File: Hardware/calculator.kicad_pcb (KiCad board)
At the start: 4 copper layers, 70.5 x 143 mm, 46 parts

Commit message: feat: update calculator engine capabilities, automate PCB manufacturing output, and refine hardware build process
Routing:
- added copper zone on B.Cu, net (none)
- added copper zone on F.Cu, net (none)
- added copper zone on In1.Cu, net (none)
- added copper zone on In2.Cu, net (none)
- removed copper zone on B.Cu, net GND
- removed copper zone on F.Cu, net GND
- removed copper zone on In1.Cu, net GND
- removed copper zone on In2.Cu, net GND

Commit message: feat: implement alpha key input support and unify error handling in RetroUIController
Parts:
- moved Disp 6.00 mm to (29.5, -125.9)
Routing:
- net P21: track 185.1 -> 51.6 mm, vias 3 -> 0
- net P20: track 89.1 -> 131.7 mm, vias 0 -> 3
- net P6: track 162.6 -> 197.1 mm, vias 4 -> 5
- net P1: track 134.6 -> 165.9 mm, vias 5 -> 4
- net P4: track 109.3 -> 132.8 mm, vias 6 -> 4
- net P10: track 173.3 -> 195.4 mm, vias 3 -> 4
- net P5: track 145.5 -> 167.1 mm, vias 3 -> 4
- net P14: track 135.2 -> 153.6 mm, vias 2 -> 1
- net P18: track 1.74 -> 19.9 mm
- net P16: track 86.2 -> 103.8 mm, vias 2 -> 1
- net GND: track 54.9 -> 67.0 mm, vias 1 -> 0
- net P0: track 129.8 -> 141.5 mm
- net P15: track 133.2 -> 142.1 mm, vias 2 -> 1
- net P9: track 141.7 -> 148.4 mm, vias 2 -> 1
- net P7: track 148.7 -> 155.3 mm, vias 2 -> 1
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- added copper zone on B.Cu, net GND
- added copper zone on F.Cu, net GND
- removed copper zone on B.Cu, net (none)
- removed copper zone on F.Cu, net (none)
- removed copper zone on In1.Cu, net (none)
- removed copper zone on In2.Cu, net (none)
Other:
- copper layers 4 -> 2

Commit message: refactor: update UI layout, adjust font rendering, and modify PCB hardware footprint configuration
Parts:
- B1, B10, B11, B12, B13, B14, B15, B16, B17, B18, B19, B2, B20, B21, B22, B23, B24, B25, B26, B27, B28, B29, B3, B30, B31, B32, B33, B34, B35, B36, B37, B4, B5, B6, B7, B8, B9: value (none) -> Tactile Switch 6x6mm
- JST1: value (none) -> JST-PH 2.0 2-Pin
- MCU1: value (none) -> RASPBERRY PI PICO
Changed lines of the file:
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@@
 	(footprint "E73:SW_TACT_ALPS_SKQGABE010"
 		(layer "F.Cu")
-		(at 17.525 -32.924999)
+		(at 39.525 -32.924999)
 		(descr "Low-profile SMD Tactile Switch, https://www.e-switch.com/product-catalog/tact/product-lines/tl3342-series-low-profile-smt-tact-switch")
 		(tags "SPST Tactile Switch")
-		(property "Reference" "B20"
+		(property "Reference" "B24"
 			(at 0 0 0)
 			(layer "F.SilkS")
@@
 			)
 		)
-		(property "Value" ""
+		(property "Value" "Tactile Switch 6x6mm"
 			(at 0 0 0)
 			(layer "F.SilkS")
@@
 			(size 1.8 1.1)
 			(layers "F.Cu" "F.Mask" "F.Paste")
-			(net "P7")
+			(net "P8")
 		)
 		(pad "NC" smd rect
@@
 	(footprint "E73:SW_TACT_ALPS_SKQGABE010"
 		(layer "F.Cu")
-		(at 39.525 -32.924999)
+		(at 17.525 -32.924999)
 		(descr "Low-profile SMD Tactile Switch, https://www.e-switch.com/product-catalog/tact/product-lines/tl3342-series-low-profile-smt-tact-switch")
 		(tags "SPST Tactile Switch")
-		(property "Reference" "B24"
+		(property "Reference" "B20"
 			(at 0 0 0)
 			(layer "F.SilkS")
@@
 			)
 		)
-		(property "Value" ""
+		(property "Value" "Tactile Switch 6x6mm"
 			(at 0 0 0)
 			(layer "F.SilkS")
@@
 			(size 1.8 1.1)
 			(layers "F.Cu" "F.Mask" "F.Paste")
-			(net "P8")
+			(net "P7")
 		)
 		(pad "NC" smd rect
@@
 			)
 		)
-		(property "Value" ""
+		(property "Value" "Tactile Switch 6x6mm"
 			(at 0 0 0)
 			(layer "F.SilkS")
@@
 			)
 		)
-		(property "Value" ""
+		(property "Value" "Tactile Switch 6x6mm"
 			(at 0 0 0)
 			(layer "F.SilkS")
@@
 			)
 		)
-		(property "Value" ""
+		(property "Value" "Tactile Switch 6x6mm"
 			(at 0 0 0)
 			(layer "F.SilkS")
@@
 			)
 		)
-		(property "Value" ""
+		(property "Value" "Tactile Switch 6x6mm"
 			(at 0 0 0)
 			(layer "F.SilkS")
@@
 			)
 		)
-		(property "Value" ""
+		(property "Value" "Tactile Switch 6x6mm"
 			(at 0 0 0)
 			(layer "F.SilkS")
@@
 			)
 		)
-		(property "Value" ""
+		(property "Value" "Tactile Switch 6x6mm"
 			(at 0 0 0)
 			(layer "F.SilkS")
@@
 			)
 		)
-		(property "Value" ""
+		(property "Value" "Tactile Switch 6x6mm"
 			(at 0 0 0)
 			(layer "F.SilkS")
@@
 			)
 		)
-		(property "Value" ""
+		(property "Value" "Tactile Switch 6x6mm"
 			(at 0 0 0)
 			(layer "F.SilkS")
@@
 			)
 		)
-		(property "Value" ""
+		(property "Value" "Tactile Switch 6x6mm"
 			(at 0 0 0)
 			(layer "F.SilkS")
@@
 			)
 		)
-		(property "Value" ""
+		(property "Value" "Tactile Switch 6x6mm"
 			(at 0 0 0)
 			(layer "F.SilkS")
@@
 	(footprint "E73:SW_TACT_ALPS_SKQGABE010"
 		(layer "F.Cu")
-		(at 17.525 -56.925)
+		(at 17.525 -44.925)
 		(descr "Low-profile SMD Tactile Switch, https://www.e-switch.com/product-catalog/tact/product-lines/tl3342-series-low-profile-smt-tact-switch")
 		(tags "SPST Tactile Switch")
-		(property "Reference" "B18"
+		(property "Reference" "B19"
 			(at 0 0 0)
 			(layer "F.SilkS")
@@
 			)
 		)
-		(property "Value" ""
+		(property "Value" "Tactile Switch 6x6mm"
 			(at 0 0 0)
 			(layer "F.SilkS")
@@
 			(size 1.8 1.1)
 			(layers "F.Cu" "F.Mask" "F.Paste")
-			(net "P5")
+			(net "P6")
 		)
 		(pad "2" smd rect
@@
 	(footprint "E73:SW_TACT_ALPS_SKQGABE010"
 		(layer "F.Cu")
-		(at 17.525 -44.925)
+		(at 17.525 -20.925)
 		(descr "Low-profile SMD Tactile Switch, https://www.e-switch.com/product-catalog/tact/product-lines/tl3342-series-low-profile-smt-tact-switch")
 		(tags "SPST Tactile Switch")
-		(property "Reference" "B19"
+		(property "Reference" "B21"
 			(at 0 0 0)
 			(layer "F.SilkS")
@@
 			)
 		)
-		(property "Value" ""
+		(property "Value" "Tactile Switch 6x6mm"
 			(at 0 0 0)
 			(layer "F.SilkS")
@@
 			(size 1.8 1.1)
 			(layers "F.Cu" "F.Mask" "F.Paste")
-			(net "P6")
+			(net "P21")
 		)
 		(pad "2" smd rect
@@
 	(footprint "E73:SW_TACT_ALPS_SKQGABE010"
 		(layer "F.Cu")
-		(at 17.525 -20.925)
+		(at 39.525 -56.925)
 		(descr "Low-profile SMD Tactile Switch, https://www.e-switch.com/product-catalog/tact/product-lines/tl3342-series-low-profile-smt-tact-switch")
 		(tags "SPST Tactile Switch")
-		(property "Reference" "B21"
+		(property "Reference" "B22"
 			(at 0 0 0)
 			(layer "F.SilkS")
@@
 			)
 		)
-		(property "Value" ""
+		(property "Value" "Tactile Switch 6x6mm"
 			(at 0 0 0)
 			(layer "F.SilkS")
@@
 			(size 1.8 1.1)
 			(layers "F.Cu" "F.Mask" "F.Paste")
-			(net "P21")
+			(net "P5")
 		)
 		(pad "2" smd rect
@@
 			(size 1.8 1.1)
 			(layers "F.Cu" "F.Mask" "F.Paste")
-			(net "P7")
+			(net "P8")
 		)
 		(pad "NC" smd rect
@@
 	(footprint "E73:SW_TACT_ALPS_SKQGABE010"
 		(layer "F.Cu")
-		(at 39.525 -56.925)
+		(at 17.525 -56.925)
 		(descr "Low-profile SMD Tactile Switch, https://www.e-switch.com/product-catalog/tact/product-lines/tl3342-series-low-profile-smt-tact-switch")
 		(tags "SPST Tactile Switch")
-		(property "Reference" "B22"
+		(property "Reference" "B18"
 			(at 0 0 0)
 			(layer "F.SilkS")
@@
 			)
 		)
-		(property "Value" ""
+		(property "Value" "Tactile Switch 6x6mm"
 			(at 0 0 0)
 			(layer "F.SilkS")
@@
 			(size 1.8 1.1)
 			(layers "F.Cu" "F.Mask" "F.Paste")
-			(net "P8")
+			(net "P7")
 		)
 		(pad "NC" smd rect
@@
 			)
 		)
-		(property "Value" ""
+		(property "Value" "Tactile Switch 6x6mm"
 			(at 0 0 0)
 			(layer "F.SilkS")
@@
 			)
 		)
-		(property "Value" ""
+		(property "Value" "Tactile Switch 6x6mm"
 			(at 0 0 0)
 			(layer "F.SilkS")
@@
 			)
 		)
-		(property "Value" ""
+		(property "Value" "Tactile Switch 6x6mm"
 			(at 0 0 0)
 			(layer "F.SilkS")
@@
 			)
 		)
-		(property "Value" ""
+		(property "Value" "Tactile Switch 6x6mm"
 			(at 0 0 0)
 			(layer "F.SilkS")
@@
 			)
 		)
-		(property "Value" ""
+		(property "Value" "Tactile Switch 6x6mm"
 			(at 0 0 0)
 			(layer "F.SilkS")
@@
 			)
 		)
-		(property "Value" ""
+		(property "Value" "Tactile Switch 6x6mm"
 			(at 0 0 0)
 			(layer "F.SilkS")
@@
 			)
 		)
-		(property "Value" ""
+		(property "Value" "Tactile Switch 6x6mm"
 			(at 0 0 0)
 			(layer "F.SilkS")
@@
 			)
 		)
-		(property "Value" ""
+		(property "Value" "Tactile Switch 6x6mm"
 			(at 0 0 0)
 			(layer "F.SilkS")
@@
 			)
 		)
-		(property "Value" ""
+		(property "Value" "Tactile Switch 6x6mm"
 			(at 0 0 0)
 			(layer "F.SilkS")
@@
 			)
 		)
-		(property "Value" ""
+		(property "Value" "Tactile Switch 6x6mm"
 			(at 0 0 0)
 			(layer "F.SilkS")
@@
 			)
 		)
-		(property "Value" ""
+		(property "Value" "Tactile Switch 6x6mm"
 			(at 0 0 0)
 			(layer "F.SilkS")
@@
 			)
 		)
-		(property "Value" ""
+		(property "Value" "Tactile Switch 6x6mm"
 			(at 0 0 0)
 			(layer "F.SilkS")
@@
 			)
 		)
-		(property "Value" ""
+		(property "Value" "Tactile Switch 6x6mm"
 			(at 0 0 0)
 			(layer "F.SilkS")
@@
 			)
 		)
-		(property "Value" ""
+		(property "Value" "Tactile Switch 6x6mm"
 			(at 0 0 0)
 			(layer "F.SilkS")
@@
 			)
 		)
-		(property "Value" ""
+		(property "Value" "Tactile Switch 6x6mm"
 			(at 0 0 0)
 			(layer "F.SilkS")
@@
 			)
 		)
-		(property "Value" ""
+		(property "Value" "Tactile Switch 6x6mm"
 			(at 0 0 0)
 			(layer "F.SilkS")
@@
 			)
 		)
-		(property "Value" ""
+		(property "Value" "Tactile Switch 6x6mm"
 			(at 0 0 0)
 			(layer "F.SilkS")
@@
 			)
 		)
-		(property "Value" ""
+		(property "Value" "Tactile Switch 6x6mm"
 			(at 0 0 0)
 			(layer "F.SilkS")
@@
 			)
 		)
-		(property "Value" ""
+		(property "Value" "Tactile Switch 6x6mm"
 			(at 0 0 0)
 			(layer "F.SilkS")
@@
 			)
 		)
-		(property "Value" ""
+		(property "Value" "Tactile Switch 6x6mm"
 			(at 0 0 0)
 			(layer "F.SilkS")
@@
 			)
 		)
-		(property "Value" ""
+		(property "Value" "Tactile Switch 6x6mm"
 			(at 0 0 0)
 			(layer "F.SilkS")
@@
 			)
 		)
-		(property "Value" ""
+		(property "Value" "JST-PH 2.0 2-Pin"
 			(at 0 0 0)
 			(layer "B.SilkS")
@@
 			)
 		)
-		(property "Value" ""
+		(property "Value" "RASPBERRY PI PICO"
 			(at 0 0 0)
 			(layer "B.SilkS")

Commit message: refactor: migrate UI display to use dedicated font scaling and add PCBWay manufacturing guidelines and BOM generation improvements
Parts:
- added FID1: Fiducial_1mm_Mask2mm, Fiducial:Fiducial_1mm_Mask2mm, F.Cu at (5.00, 140.0)
- added FID2: Fiducial_1mm_Mask2mm, Fiducial:Fiducial_1mm_Mask2mm, F.Cu at (60.0, 140.0)
- added FID3: Fiducial_1mm_Mask2mm, Fiducial:Fiducial_1mm_Mask2mm, F.Cu at (60.0, 20.0)
- added J1: Sharp_LCD_10Pin, Connector_FFC-FPC:Hirose_FH12-10S-0.5SH_1x10-1MP_P0.50mm_Horizontal, F.Cu at (45.0, -130.0)
- added REF**: MountingHole_3.2mm_M3, MountingHole:MountingHole_3.2mm_M3, F.Cu at (18.9, -144.1)
- added REF**: MountingHole_3.2mm_M3, MountingHole:MountingHole_3.2mm_M3, F.Cu at (18.9, -16.9)
- added REF**: MountingHole_3.2mm_M3, MountingHole:MountingHole_3.2mm_M3, F.Cu at (71.6, -144.1)
- added REF**: MountingHole_3.2mm_M3, MountingHole:MountingHole_3.2mm_M3, F.Cu at (71.6, -16.9)
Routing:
- net (no net): track 0.00 -> 254.2 mm, vias 0 -> 10
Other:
- board size 70.5 x 143 mm -> 66.7 x 137.1 mm

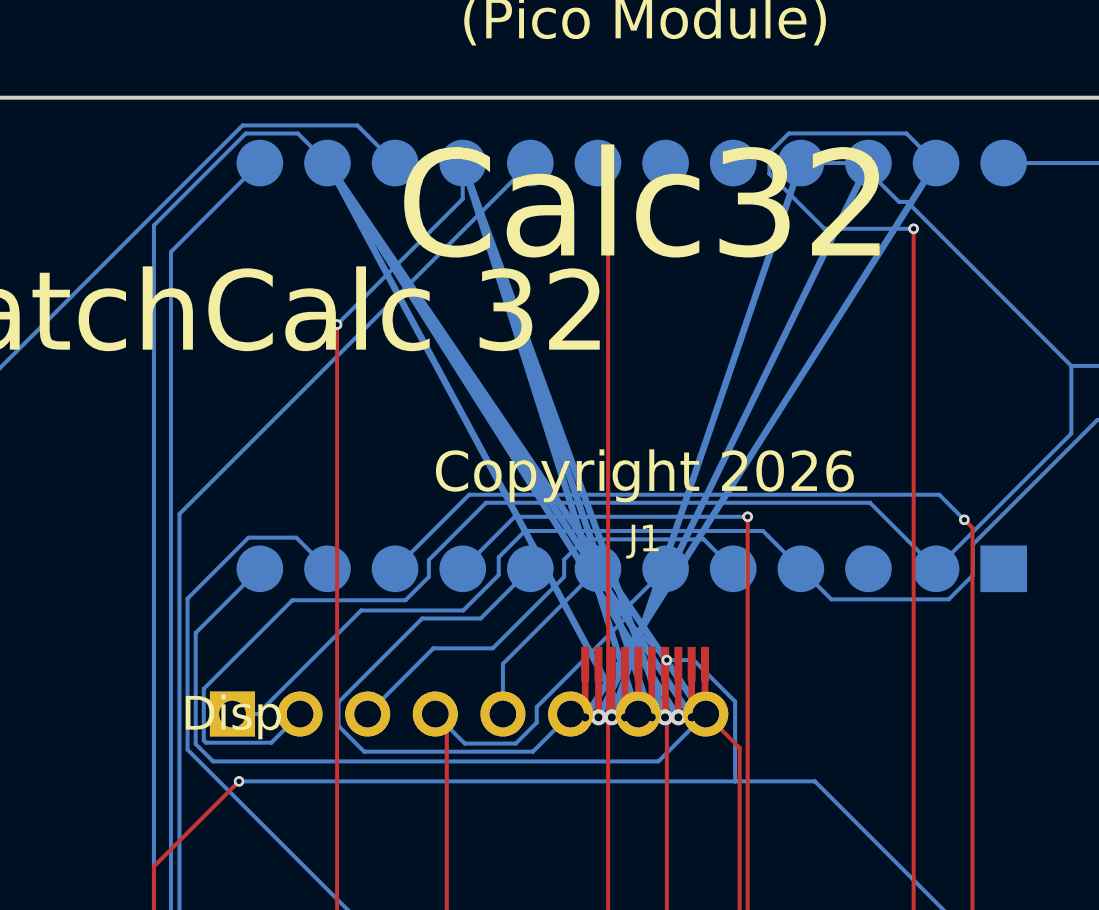
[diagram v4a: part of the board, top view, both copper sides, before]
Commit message: feat: replace E-Ink footprint with Sharp LCD connector and update calculator key map with new navigation actions
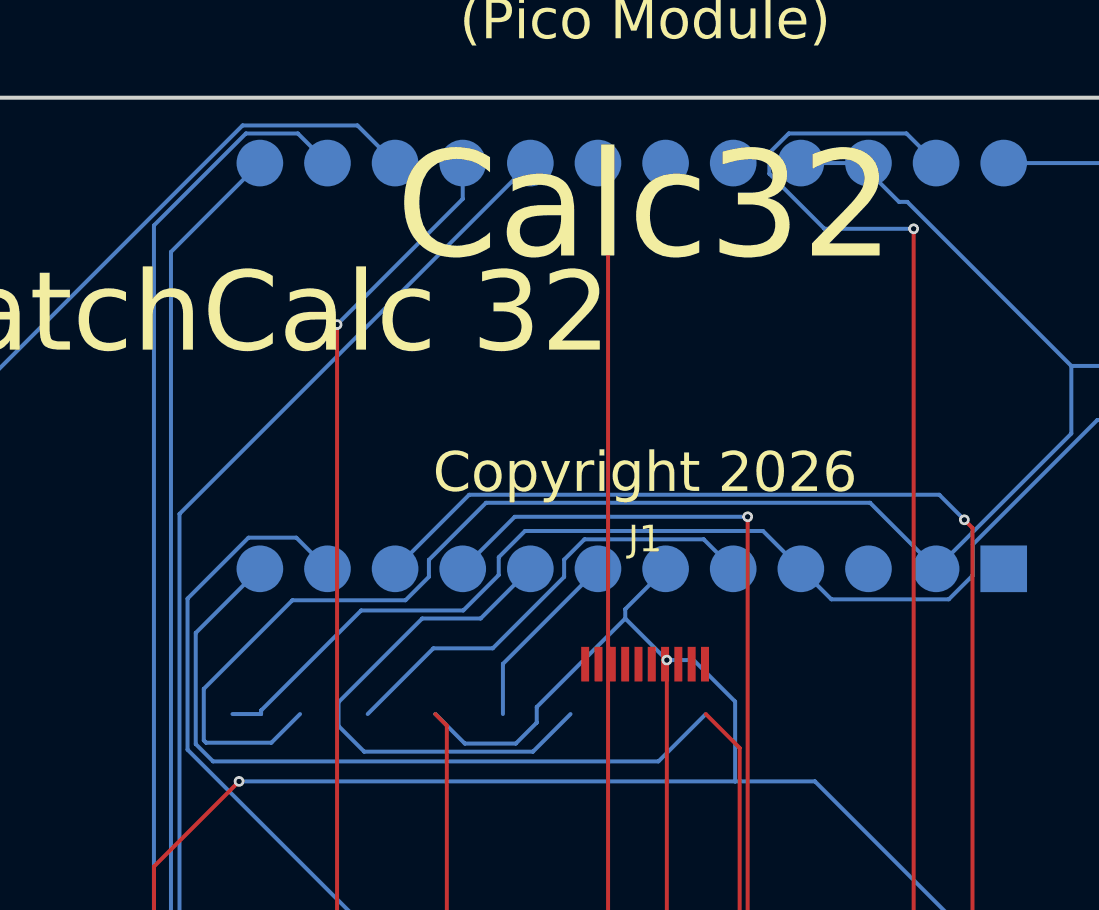
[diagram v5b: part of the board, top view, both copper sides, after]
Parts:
- removed Disp: E-Ink, 
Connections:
- J1 pad 1: (no net) -> P21
- J1 pad 10: (no net) -> GND
- J1 pad 2: (no net) -> P20
- J1 pad 3: (no net) -> P19
- J1 pad 4: (no net) -> P18
- J1 pad 5: (no net) -> GND
- J1 pad 6: (no net) -> VCC
- J1 pad 7: (no net) -> VCC
- J1 pad 8: (no net) -> GND
- J1 pad 9: (no net) -> GND
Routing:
- net (no net): track 254.2 -> 0.00 mm, vias 10 -> 0

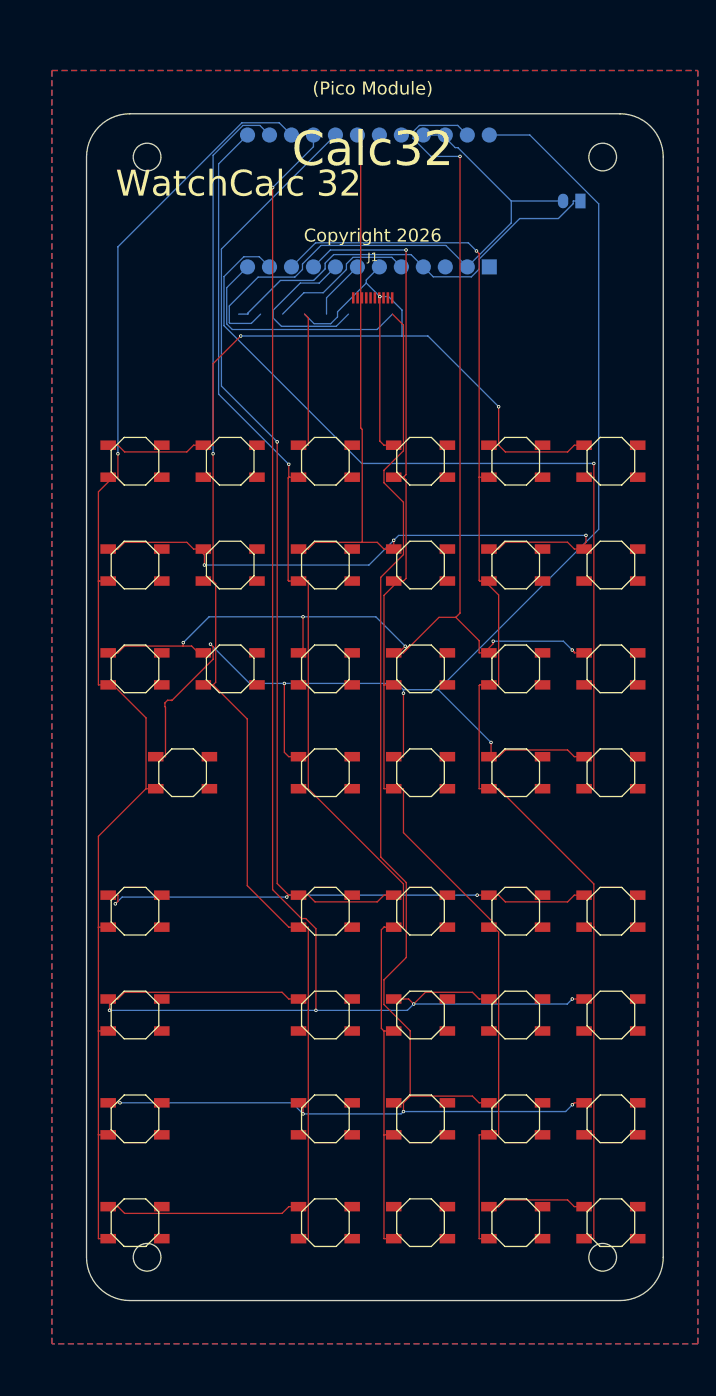
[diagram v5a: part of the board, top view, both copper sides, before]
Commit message: feat: update hardware design layout tools and expand calculator UI and testing frameworks
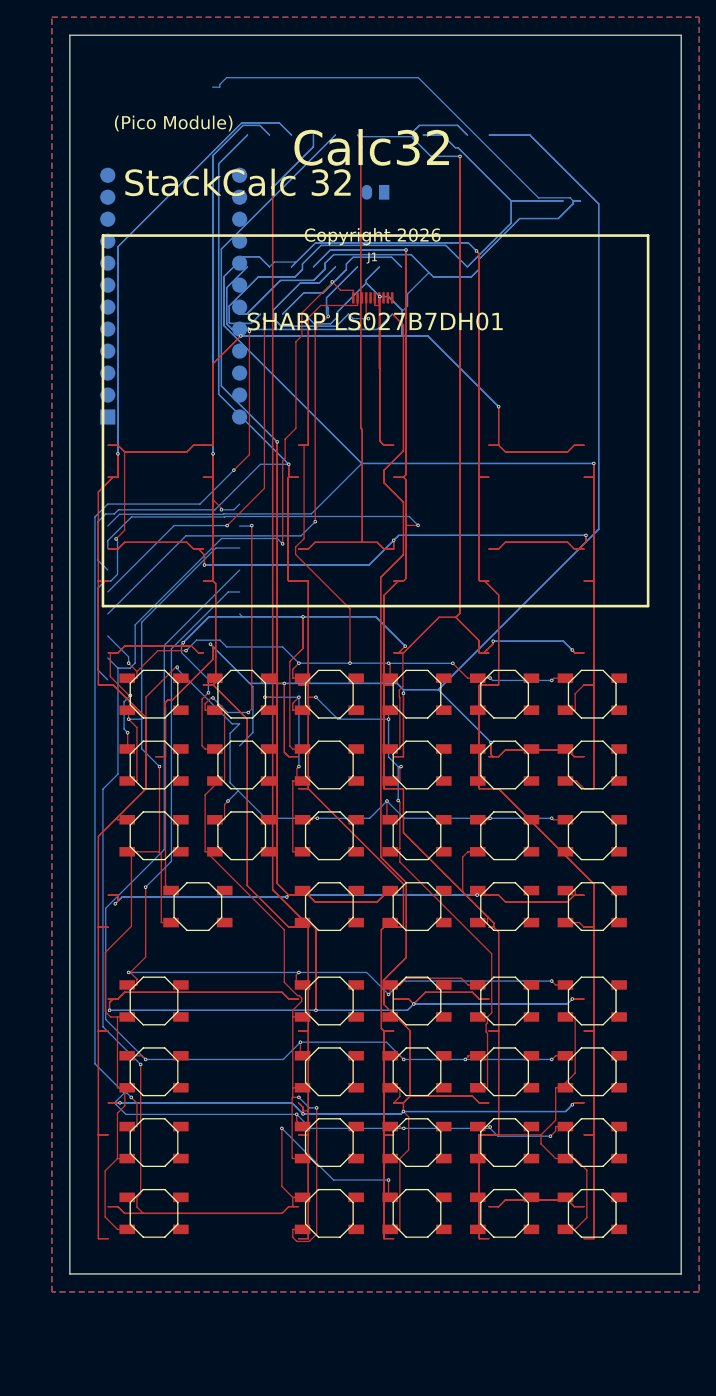
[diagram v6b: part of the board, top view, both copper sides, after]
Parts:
- removed REF** (x4): MountingHole_3.2mm_M3, MountingHole:MountingHole_3.2mm_M3
- moved SOFT1 27.0 mm to (19.7, -82.0)
- moved SOFT6 27.0 mm to (70.4, -82.0)
- moved SOFT2 27.0 mm to (29.9, -82.0)
- moved SOFT5 27.0 mm to (60.2, -82.0)
- moved SOFT3 26.9 mm to (40.0, -82.0)
- moved SOFT4 26.9 mm to (50.1, -82.0)
- moved MCU1 25.0 mm to (22.0, -128.0), turned to 90 degrees
- moved B3 23.2 mm to (19.7, -73.8)
- moved B17 23.2 mm to (70.4, -73.8)
- moved B5 23.1 mm to (29.9, -73.8)
- moved B14 23.1 mm to (60.2, -73.8)
- moved B8 23.1 mm to (40.0, -73.8)
- moved B11 23.1 mm to (50.1, -73.8)
- moved JST1 22.7 mm to (45.3, -140.0)
- moved B2 19.4 mm to (19.7, -65.6)
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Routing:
- net P9: track 148.4 -> 1076.5 mm, vias 1 -> 14
- net P1: track 165.9 -> 694.3 mm, vias 4 -> 8
- net P4: track 132.8 -> 608.4 mm, vias 4 -> 13
- net P16: track 103.8 -> 560.2 mm, vias 1 -> 2
- net VCC: track 48.4 -> 419.6 mm, vias 0 -> 4
- net P15: track 142.1 -> 394.4 mm, vias 1 -> 5
- net P0: track 141.5 -> 389.8 mm, vias 6 -> 7
- net P14: track 153.6 -> 370.0 mm, vias 1 -> 2
- net P21: track 51.6 -> 264.6 mm, vias 0 -> 5
- net P6: track 197.1 -> 122.6 mm
- net P18: track 19.9 -> 89.0 mm, vias 0 -> 3
- net GND: track 67.0 -> 134.1 mm
- net P19: track 6.93 -> 67.9 mm, vias 0 -> 2
- net P5: track 167.1 -> 119.7 mm, vias 4 -> 5
- net P7: track 155.3 -> 118.6 mm, vias 1 -> 2
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- added copper zone on B.Cu, net (none)
- added copper zone on F.Cu, net (none)
- removed copper zone on B.Cu, net GND
- removed copper zone on F.Cu, net GND
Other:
- board size 66.7 x 137.1 mm -> 70.7 x 143.2 mm
- board text added: "SHARP LS027B7DH01"
- board text added: "StackCalc 32"
- board text removed: "WatchCalc 32"
